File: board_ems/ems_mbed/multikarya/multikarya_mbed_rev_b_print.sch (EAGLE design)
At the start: 156 parts, among them IC1 SIM900, IC2 74HC595D, IC3 74HC595D, IC4 ADE7758RW, J5 POWER_JACKPTH, U2 W5500

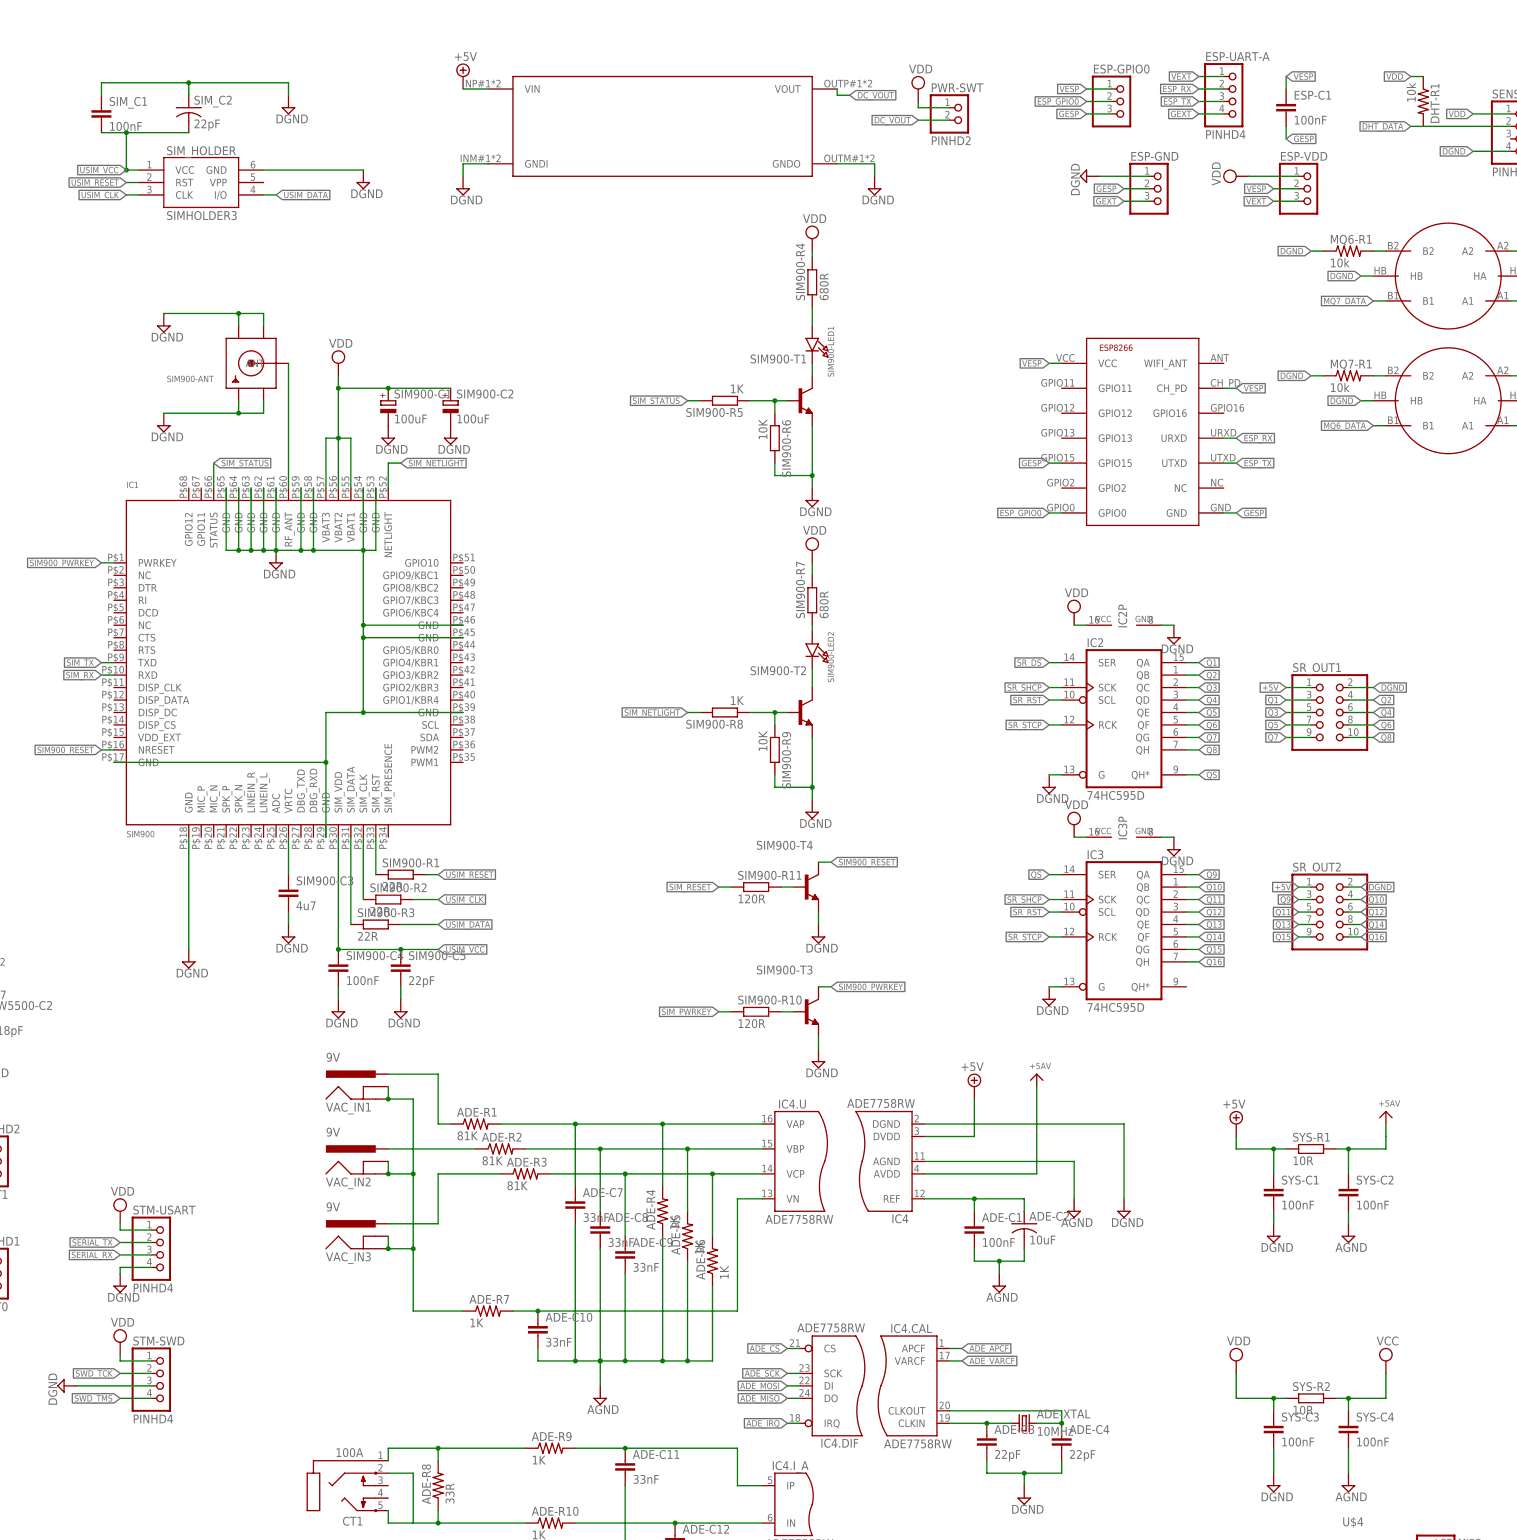
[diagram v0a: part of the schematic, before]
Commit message: add doc for SLA
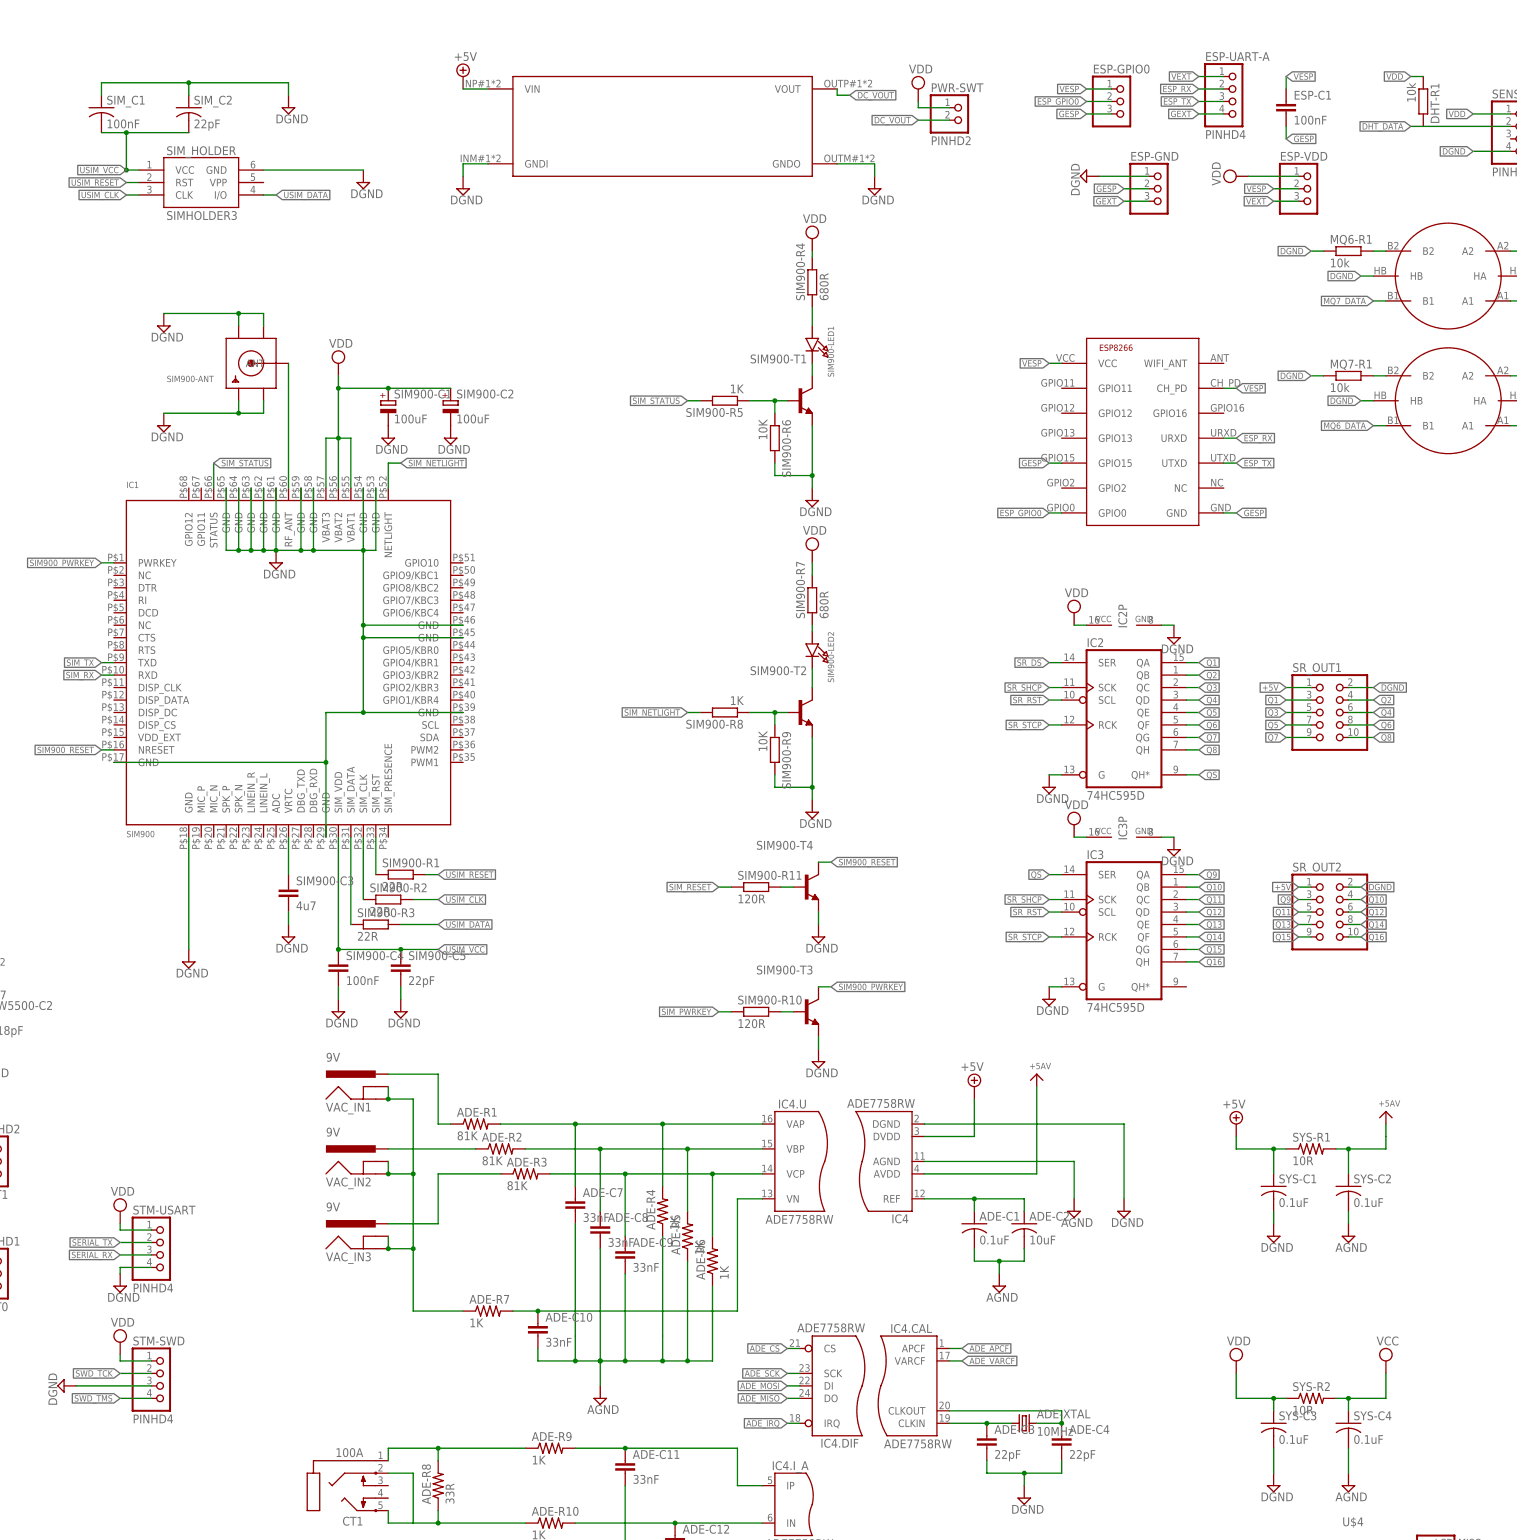
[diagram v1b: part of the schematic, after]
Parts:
- ADE-C1, SYS-C1, SYS-C2, SYS-C3, SYS-C4: value 100nF -> 0.1uF; device rcl:C-EUC0603 -> rcl:C-USC0603
- DHT-R1, MQ6-R1, MQ7-R1: device rcl:R-US_R0603 -> resistor:R-EU_R0603
- SIM_C1: device rcl:C-EUC0603 -> rcl:C-USC0603K
- SYS-R1, SYS-R2: device rcl:R-EU_R0603 -> SparkFun-Passives:RESISTOR0603-RES
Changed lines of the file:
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@@
 <setting verticaltext="up"/>
 </settings>
-<grid distance="0.1" unitdist="inch" unit="inch" style="lines" multiple="1" display="no" altdistance="0.01" altunitdist="inch" altunit="inch"/>
+<grid distance="0.05" unitdist="inch" unit="inch" style="lines" multiple="1" display="no" altdistance="0.01" altunitdist="inch" altunit="inch"/>
 <layers>
 <layer number="1" name="Top" color="4" fill="1" visible="no" active="no"/>
@@
 <part name="SUPPLY20" library="supply2" deviceset="DGND" device=""/>
 <part name="SIM_HOLDER" library="SparkFun" deviceset="SIMHOLDER3" device=""/>
-<part name="SIM_C1" library="rcl" deviceset="C-EU" device="C0603" value="100nF"/>
+<part name="SIM_C1" library="rcl" deviceset="C-US" device="C0603K" value="100nF"/>
 <part name="SIM_C2" library="rcl" deviceset="C-US" device="C0603K" value="22pF"/>
 <part name="DCDC-3.5V" library="bontor" deviceset="DCDCMODULE_SMALL" device=""/>
@@
 <part name="SUPPLY65" library="supply2" deviceset="AGND" device=""/>
 <part name="SUPPLY66" library="supply2" deviceset="AGND" device=""/>
-<part name="ADE-C1" library="rcl" deviceset="C-EU" device="C0603" value="100nF"/>
+<part name="ADE-C1" library="rcl" deviceset="C-US" device="C0603" value="0.1uF"/>
 <part name="ADE-C2" library="rcl" deviceset="C-US" device="C0805K" value="10uF"/>
 <part name="SUPPLY67" library="supply2" deviceset="AGND" device=""/>
@@
 <part name="SUPPLY85" library="supply2" deviceset="DGND" device=""/>
 <part name="SUPPLY86" library="supply2" deviceset="AGND" device=""/>
-<part name="SYS-R1" library="rcl" deviceset="R-EU_" device="R0603" value="10R"/>
-<part name="SYS-C1" library="rcl" deviceset="C-EU" device="C0603" value="100nF"/>
-<part name="SYS-C2" library="rcl" deviceset="C-EU" device="C0603" value="100nF"/>
+<part name="SYS-R1" library="SparkFun-Passives" deviceset="RESISTOR" device="0603-RES" value="10R"/>
+<part name="SYS-C1" library="rcl" deviceset="C-US" device="C0603" value="0.1uF"/>
+<part name="SYS-C2" library="rcl" deviceset="C-US" device="C0603" value="0.1uF"/>
 <part name="SUPPLY87" library="supply2" deviceset="AGND" device=""/>
 <part name="SUPPLY88" library="supply2" deviceset="DGND" device=""/>
@@
 <part name="SUPPLY78" library="supply2" deviceset="DGND" device=""/>
 <part name="SUPPLY95" library="supply2" deviceset="DGND" device=""/>
-<part name="SYS-R2" library="rcl" deviceset="R-EU_" device="R0603" value="10R"/>
-<part name="SYS-C3" library="rcl" deviceset="C-EU" device="C0603" value="100nF"/>
-<part name="SYS-C4" library="rcl" deviceset="C-EU" device="C0603" value="100nF"/>
+<part name="SYS-R2" library="SparkFun-Passives" deviceset="RESISTOR" device="0603-RES" value="10R"/>
+<part name="SYS-C3" library="rcl" deviceset="C-US" device="C0603" value="0.1uF"/>
+<part name="SYS-C4" library="rcl" deviceset="C-US" device="C0603" value="0.1uF"/>
 <part name="SUPPLY100" library="supply2" deviceset="AGND" device=""/>
 <part name="SUPPLY102" library="supply2" deviceset="DGND" device=""/>
@@
 <part name="SR_OUT1" library="pinhead" deviceset="PINHD-2X5" device="/90"/>
 <part name="SR_OUT2" library="pinhead" deviceset="PINHD-2X5" device="/90"/>
-<part name="DHT-R1" library="rcl" deviceset="R-US_" device="R0603" value="10k"/>
+<part name="DHT-R1" library="resistor" deviceset="R-EU_" device="R0603" value="10k"/>
 <part name="SENSOR-MQ6" library="SparkFun-Sensors" deviceset="METHANE_SENSOR" device=""/>
 <part name="SENSOR-MQ7" library="SparkFun-Sensors" deviceset="METHANE_SENSOR" device=""/>
-<part name="MQ6-R1" library="rcl" deviceset="R-US_" device="R0603" value="10k"/>
-<part name="MQ7-R1" library="rcl" deviceset="R-US_" device="R0603" value="10k"/>
+<part name="MQ6-R1" library="resistor" deviceset="R-EU_" device="R0603" value="10k"/>
+<part name="MQ7-R1" library="resistor" deviceset="R-EU_" device="R0603" value="10k"/>
 <part name="U$4" library="TFT_LCD_2.2" deviceset="TFT_LCD_2.2+F_CS" device=""/>
 <part name="SUPPLY80" library="supply2" deviceset="DGND" device=""/>
